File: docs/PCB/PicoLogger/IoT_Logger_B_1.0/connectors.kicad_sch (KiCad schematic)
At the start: 10 parts, among them J10 Modbus, J3 USB-C, J4 Sensor, J5 LCD 16x2, J6 Additional, J7 SPI, J8 Relay, J9 CAN, U7 TPD2EUSB30

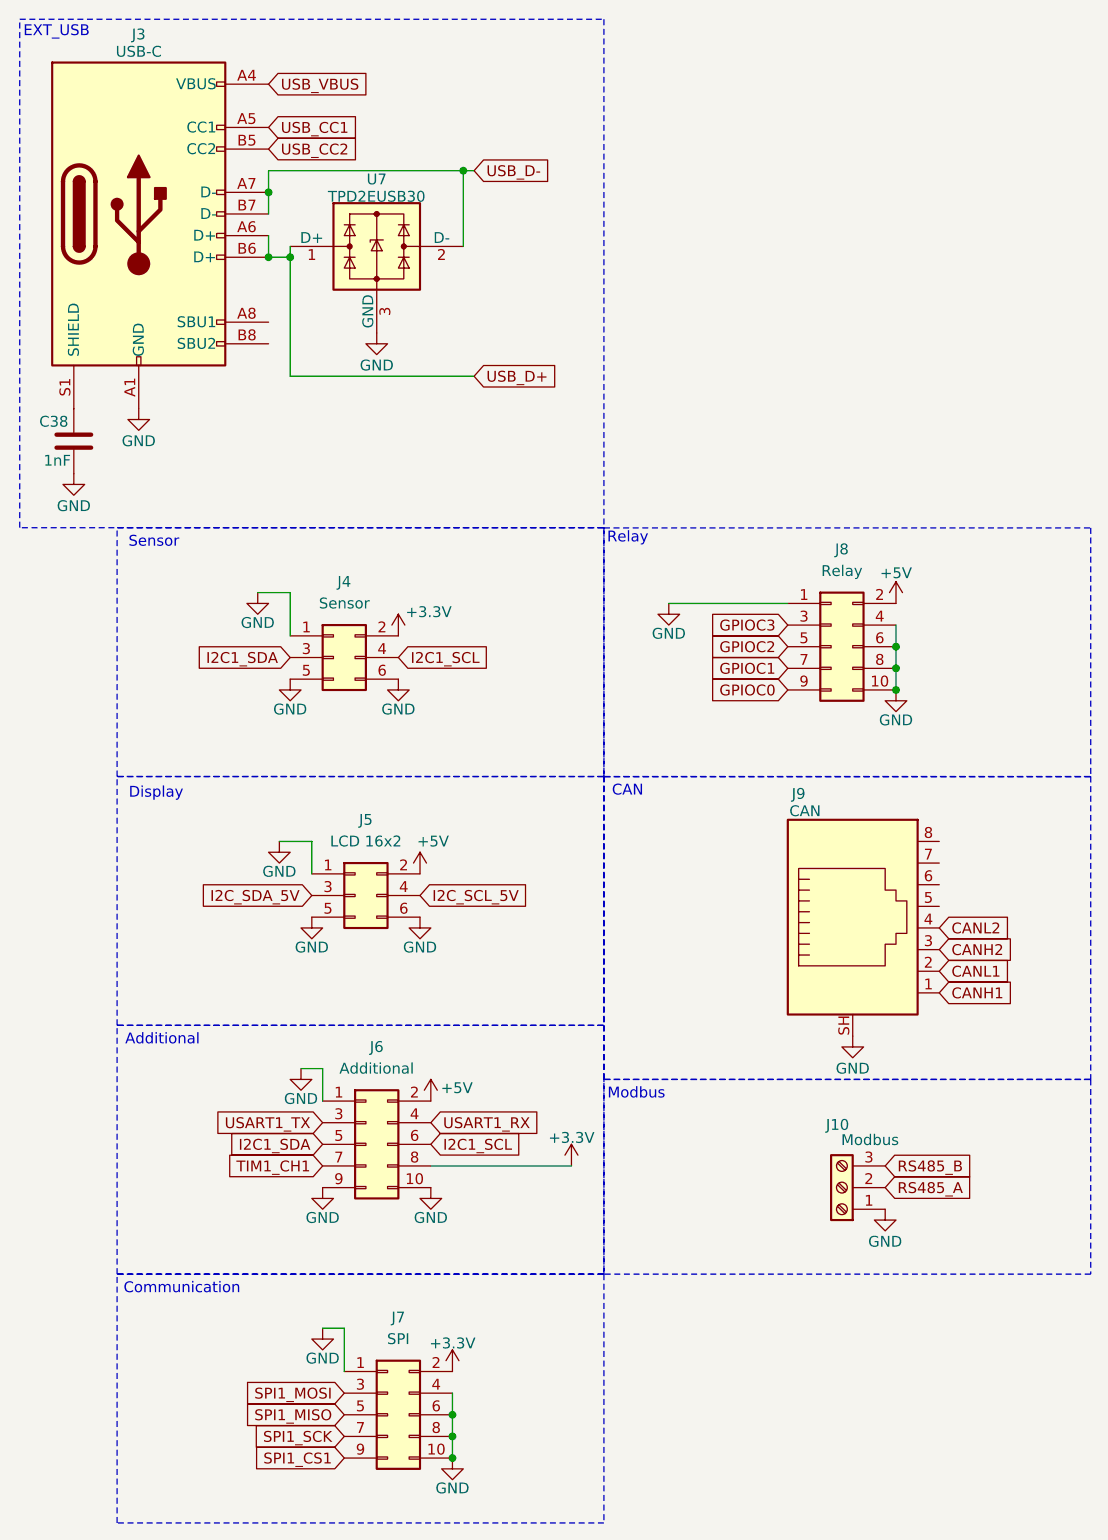
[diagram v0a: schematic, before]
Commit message: Logger IoT B and C production files generated, backend and frontend prepared for new logger type.
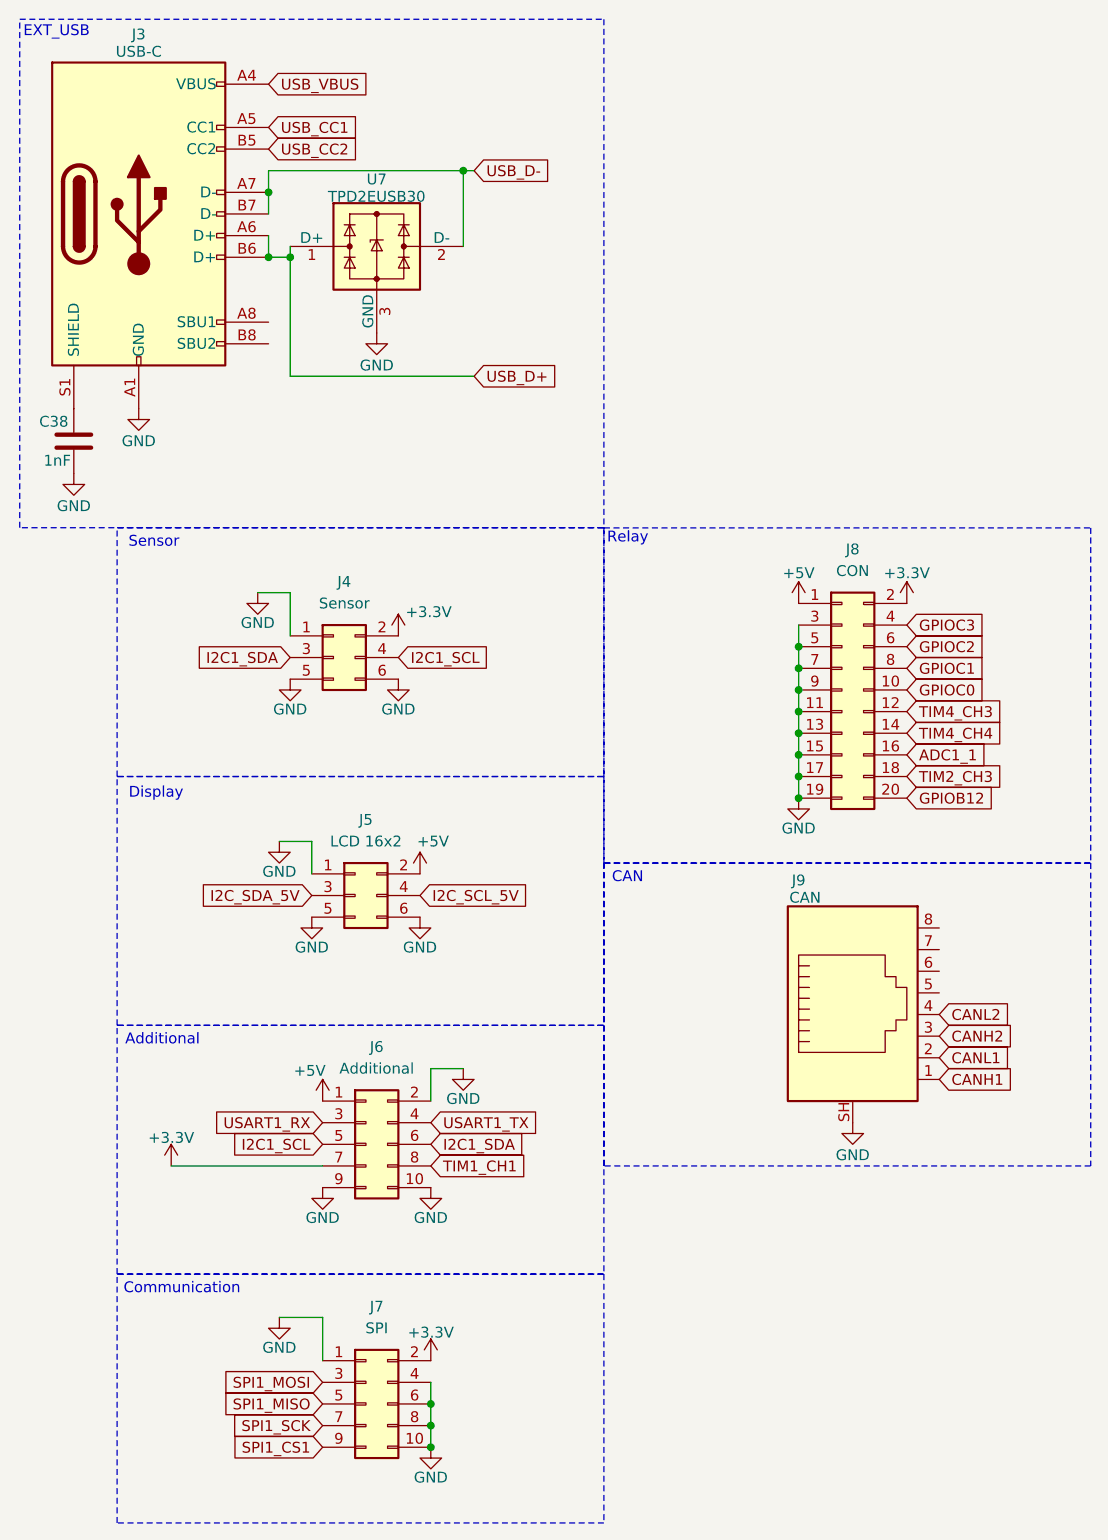
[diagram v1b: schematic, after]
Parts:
- removed J10: Modbus, TerminalBlock_Phoenix:TerminalBlock_Phoenix_MKDS-1,5-3_1x03_P5.00mm_Horizontal, symbol Connector:Screw_Terminal_01x03
- removed J8: Relay, Connector_IDC:IDC-Header_2x05_P2.54mm_Vertical, symbol Connector_Generic:Conn_02x05_Odd_Even
- added J8: CON, Connector_PinSocket_2.54mm:PinSocket_2x10_P2.54mm_Vertical, symbol Connector_Generic:Conn_02x10_Odd_Even
- J6: footprint Connector_IDC:IDC-Header_2x05_P2.54mm_Vertical -> Connector_PinSocket_2.54mm:PinSocket_2x05_P2.54mm_Vertical
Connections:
- net +3.3V: now also J6.7 (Pin_7), J8.2 (Pin_2); no longer J6.8 (Pin_8)
- net +5V: now also J6.1 (Pin_1), J8.1 (Pin_1); no longer J6.2 (Pin_2)
- net GND: now also J6.2 (Pin_2), J8.11 (Pin_11), J8.13 (Pin_13), J8.15 (Pin_15), J8.17 (Pin_17), J8.19 (Pin_19), J8.3 (Pin_3), J8.5 (Pin_5), J8.7 (Pin_7), J8.9 (Pin_9); no longer J6.1 (Pin_1)
- net GPIOC0: now also J8.10 (Pin_10)
- net GPIOC1: now also J8.8 (Pin_8)
- net GPIOC2: now also J8.6 (Pin_6)
- net GPIOC3: now also J8.4 (Pin_4)
- net I2C1_SCL: now also J6.5 (Pin_5); no longer J6.6 (Pin_6)
- net I2C1_SDA: now also J6.6 (Pin_6); no longer J6.5 (Pin_5)
- net TIM1_CH1: now also J6.8 (Pin_8); no longer J6.7 (Pin_7)
- net USART1_RX: now also J6.3 (Pin_3); no longer J6.4 (Pin_4)
- net USART1_TX: now also J6.4 (Pin_4); no longer J6.3 (Pin_3)
- new net ADC1_1: J8.16 (Pin_16)
- new net GPIOB12: J8.20 (Pin_20)
- new net TIM2_CH3: J8.18 (Pin_18)
- new net TIM4_CH3: J8.12 (Pin_12)
- new net TIM4_CH4: J8.14 (Pin_14)
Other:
- note removed: "Modbus"
- moved on the sheet: J7, J9

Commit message: Code added, documentation review.
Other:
- moved on the sheet: J8, J9
